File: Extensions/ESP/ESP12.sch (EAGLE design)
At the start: 8 parts, among them IC1 REG1117, J1 RASPBERRYPI-40-PIN-GPIO_PTH_N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

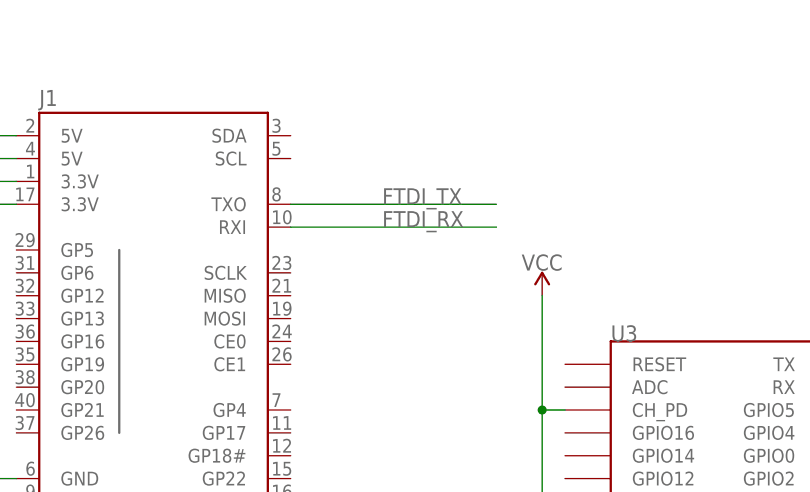
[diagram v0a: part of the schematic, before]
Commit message: Updated ESP expansion; now teledildonics and swapped TX and RX lines
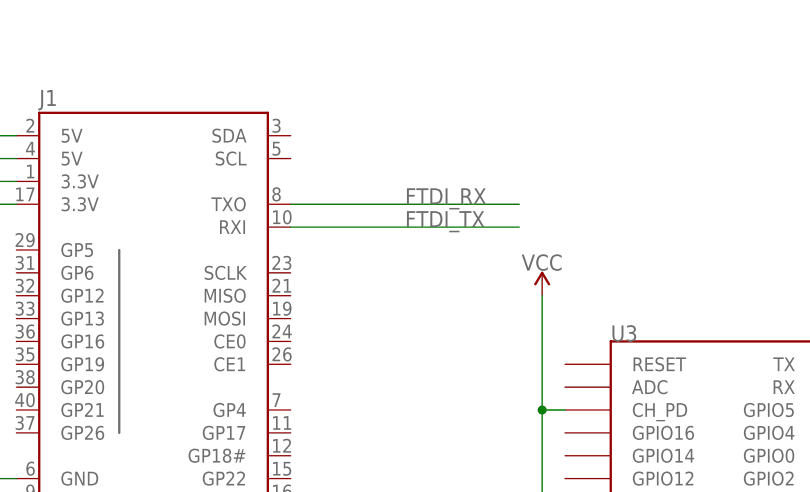
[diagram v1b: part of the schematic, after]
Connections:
- net FTDI_RX: now also J1.TXO; no longer J1.RXI
- net FTDI_TX: now also J1.RXI; no longer J1.TXO
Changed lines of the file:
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@@
 </segment>
 <segment>
-<pinref part="J1" gate="G$1" pin="TXO"/>
-<wire x1="38.1" y1="63.5" x2="60.96" y2="63.5" width="0.1524" layer="91"/>
-<label x="48.26" y="63.5" size="1.778" layer="95"/>
+<pinref part="J1" gate="G$1" pin="RXI"/>
+<wire x1="38.1" y1="60.96" x2="63.5" y2="60.96" width="0.1524" layer="91"/>
+<label x="50.8" y="60.96" size="1.778" layer="95"/>
 </segment>
 </net>
@@
 </segment>
 <segment>
-<pinref part="J1" gate="G$1" pin="RXI"/>
-<wire x1="38.1" y1="60.96" x2="60.96" y2="60.96" width="0.1524" layer="91"/>
-<label x="48.26" y="60.96" size="1.778" layer="95"/>
+<pinref part="J1" gate="G$1" pin="TXO"/>
+<wire x1="38.1" y1="63.5" x2="63.5" y2="63.5" width="0.1524" layer="91"/>
+<label x="50.8" y="63.5" size="1.778" layer="95"/>
 </segment>
 </net>
